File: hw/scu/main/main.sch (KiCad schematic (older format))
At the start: 27 parts, among them J1 Conn_01x03_MountingPin, J2 Conn_01x06_MountingPin, SW1 SW_Push, U1 STM32F072C8Tx, U2 LM3670MF, U3 LP5907MFX-3.3

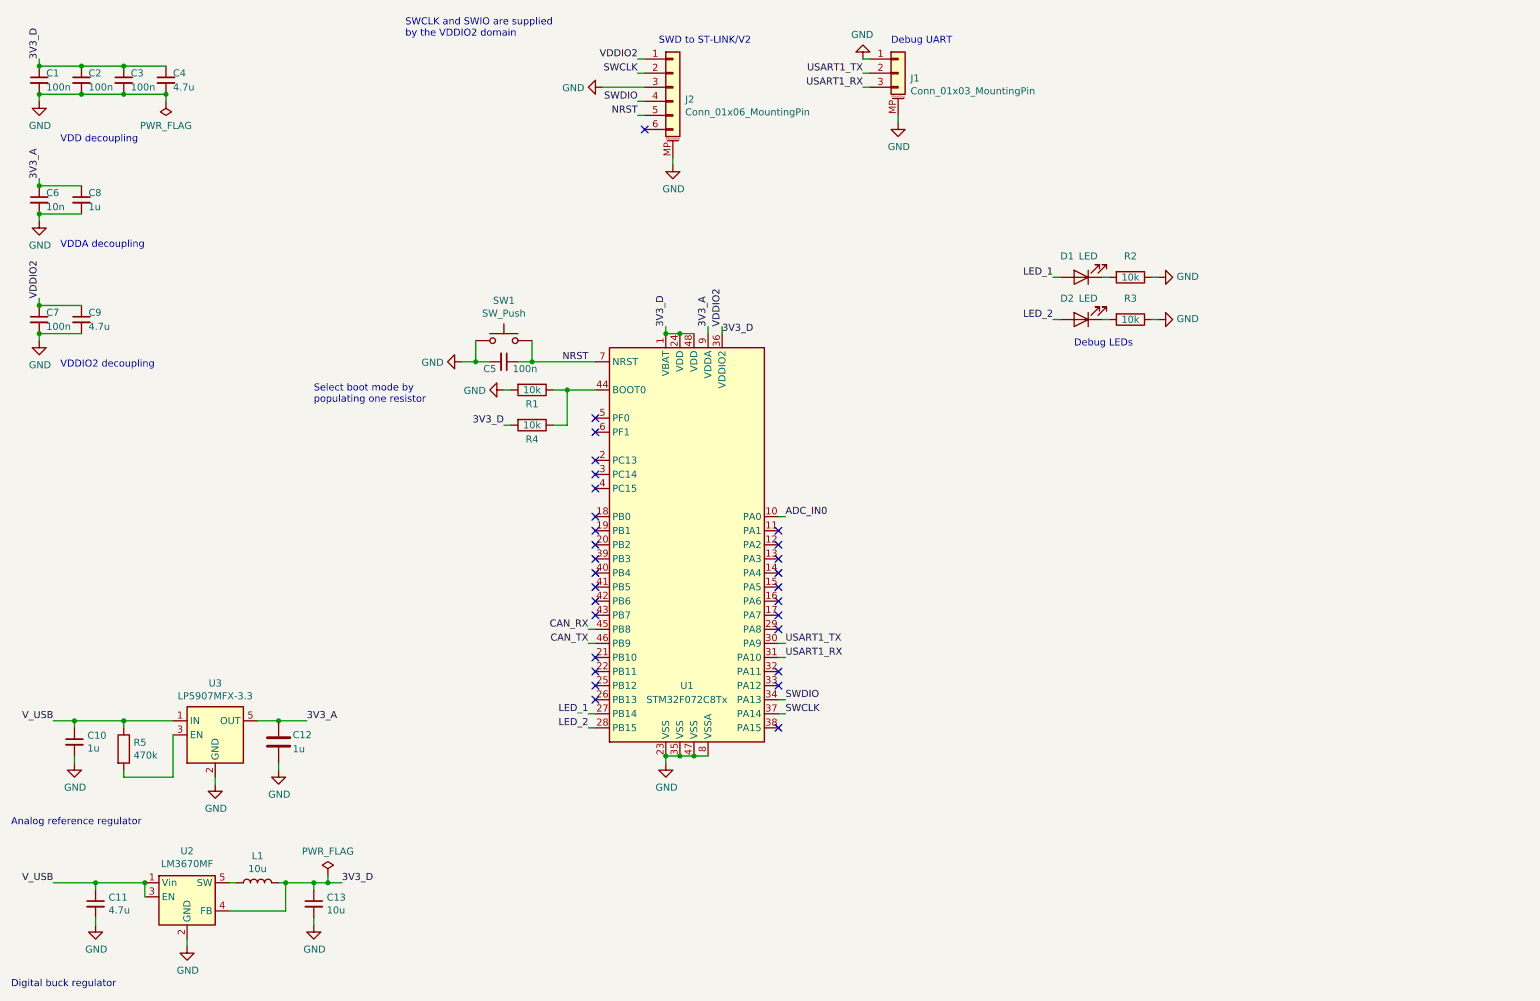
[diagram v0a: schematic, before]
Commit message: Add HSE crystal
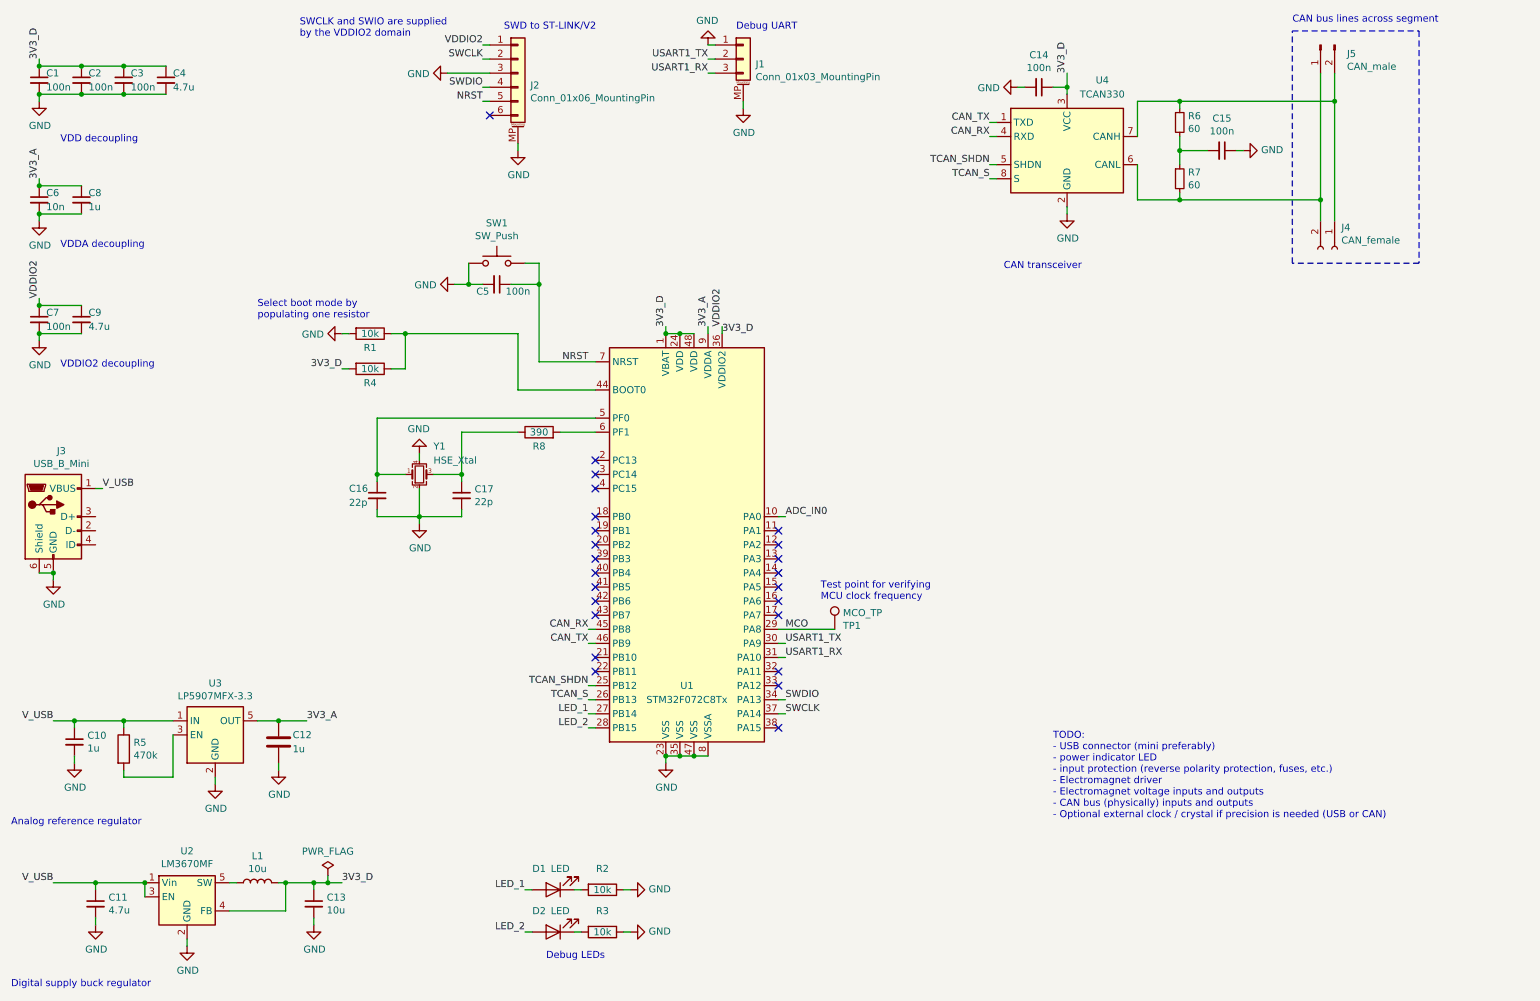
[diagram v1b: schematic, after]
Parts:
- added C14, C15: 100n, Capacitor_SMD:C_0603_1608Metric, symbol Device:C_Small
- added C16, C17: 22p, symbol Device:C_Small
- added J3: USB_B_Mini, Connector_USB:USB_Mini-B_Wuerth_65100516121_Horizontal, symbol Connector:USB_B_Mini
- added J4: CAN_female, symbol Connector:Conn_01x02_Female
- added J5: CAN_male, symbol Connector:Conn_01x02_Male
- added R6, R7: 60, Resistor_SMD:R_0603_1608Metric, symbol Device:R_Small
- added R8: 390, symbol Device:R
- added TP1: MCO_TP, symbol Connector:TestPoint
- added U4: TCAN330, Package_TO_SOT_SMD:TSOT-23-8, symbol Interface_CAN_LIN:TCAN330
- added Y1: HSE_Xtal, symbol Device:Crystal_GND24_Small
- C10, C11, C12, C13: footprint (none) -> Capacitor_SMD:C_0603_1608Metric
- L1: footprint (none) -> Inductor_SMD:L_0603_1608Metric
- R5: footprint (none) -> Resistor_SMD:R_0603_1608Metric
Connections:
- net 3V3_D: now also C14.1, U4.3 (VCC)
- net CAN_RX: now also U4.4 (RXD)
- net CAN_TX: now also U4.1 (TXD)
- net GND: now also C14.2, C15.1, C16.2, C17.2, J3.5 (GND), J3.6 (Shield), U4.2 (GND), Y1.2, Y1.4
- net V_USB: now also J3.1 (VBUS)
- net TCAN_SHDN: now reaches U1.25 (PB12)
- net TCAN_SHDN: now also U4.5 (SHDN)
- net TCAN_S: now reaches U1.26 (PB13)
- net TCAN_S: now also U4.8 (S)
- net MCO: now reaches U1.29 (PA8)
- net MCO: now also TP1.1
- net at U1.5 (PF0): now also C16.1, Y1.1
- net at U1.6 (PF1): now also R8.2
- new net: J4.2 (Pin_2), J5.1 (Pin_1), R7.2, U4.6 (CANL)
- new net: J4.1 (Pin_1), J5.2 (Pin_2), R6.1, U4.7 (CANH)
- new net: C15.2, R6.2, R7.1
- new net: C17.1, R8.1, Y1.3
- no-connect marks 29 -> 24
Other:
- note added: "CAN bus lines across segment"
- note added: "CAN transceiver"
- note added: "Digital supply buck regulator"
- note added: "TODO:\n- USB connector (mini preferably)\n- power indicator LED\n- input protection (reverse polarity protection, fuses, etc.)\n- Electromagnet driver\n- Electromagnet voltage inputs and outputs\n- CAN bus (physically) inputs and outputs\n- Optional external clock / crystal if precision is needed (USB or CAN)"
- note added: "Test point for verifying\nMCU clock frequency"
- note removed: "Digital buck regulator"
- moved on the sheet: C5, D1, D2, J1, J2, R1, R2, R3, R4, SW1
